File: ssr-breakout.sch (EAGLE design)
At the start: 15 parts, among them U1 DS2413P

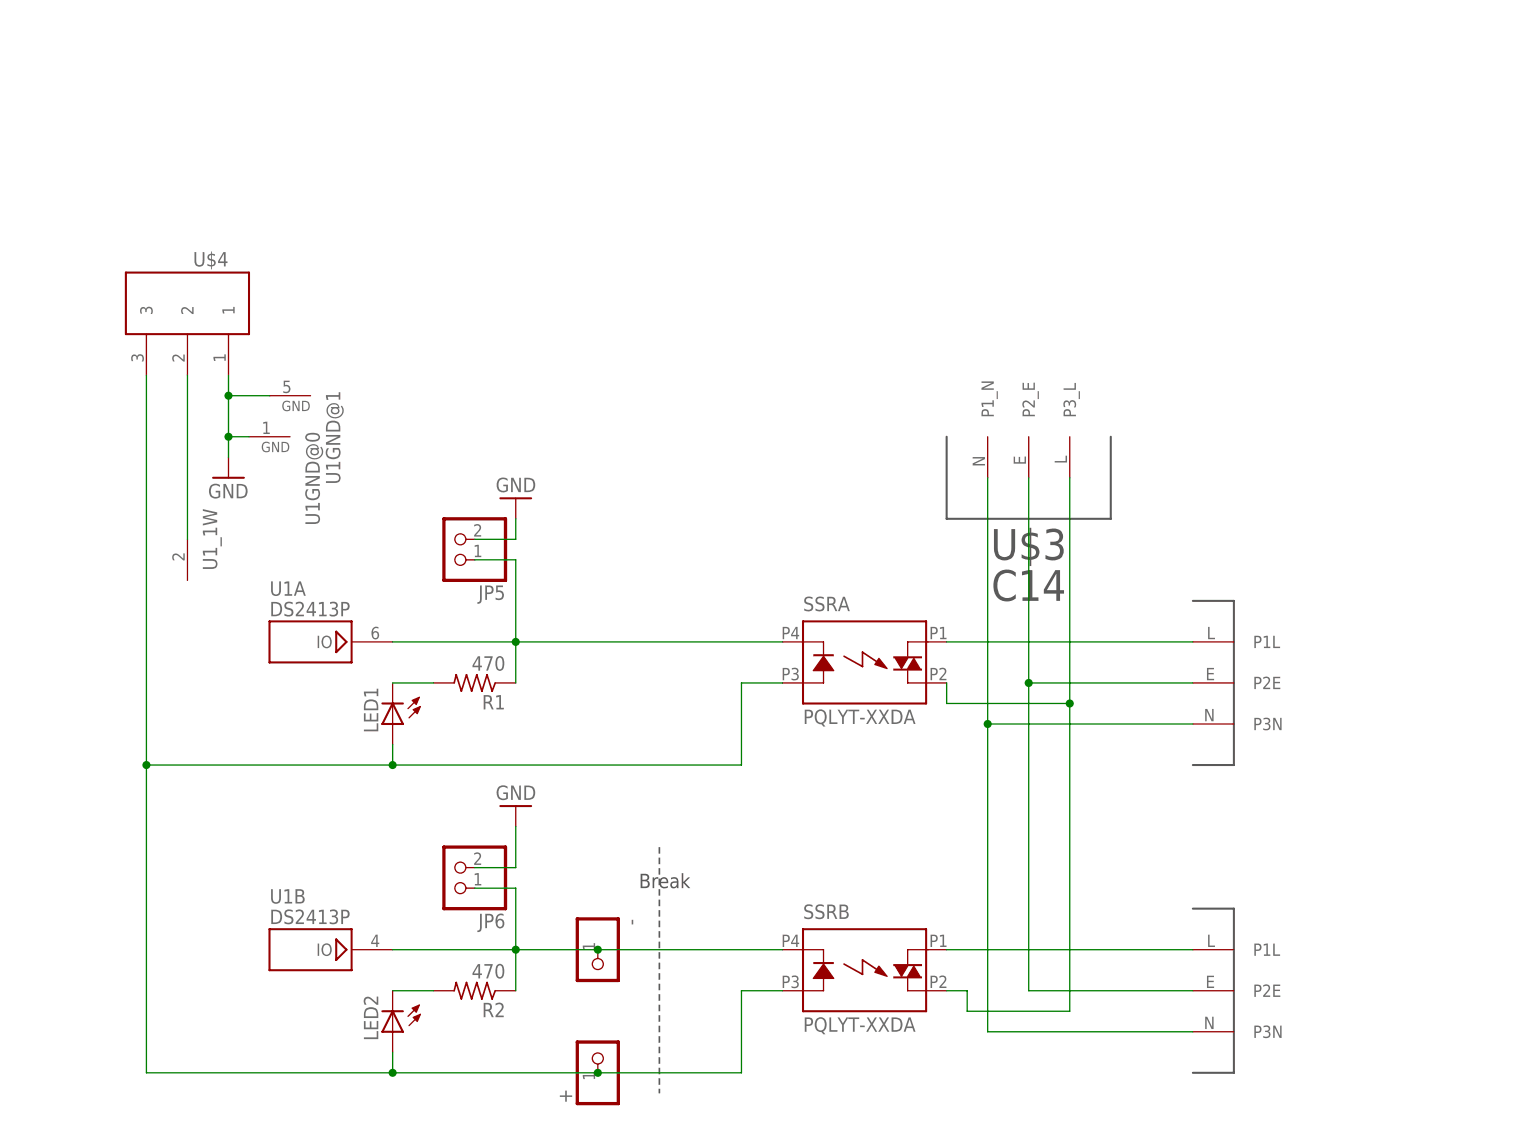
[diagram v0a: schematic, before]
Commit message: Small updates to layout to fit PQLYT SSR
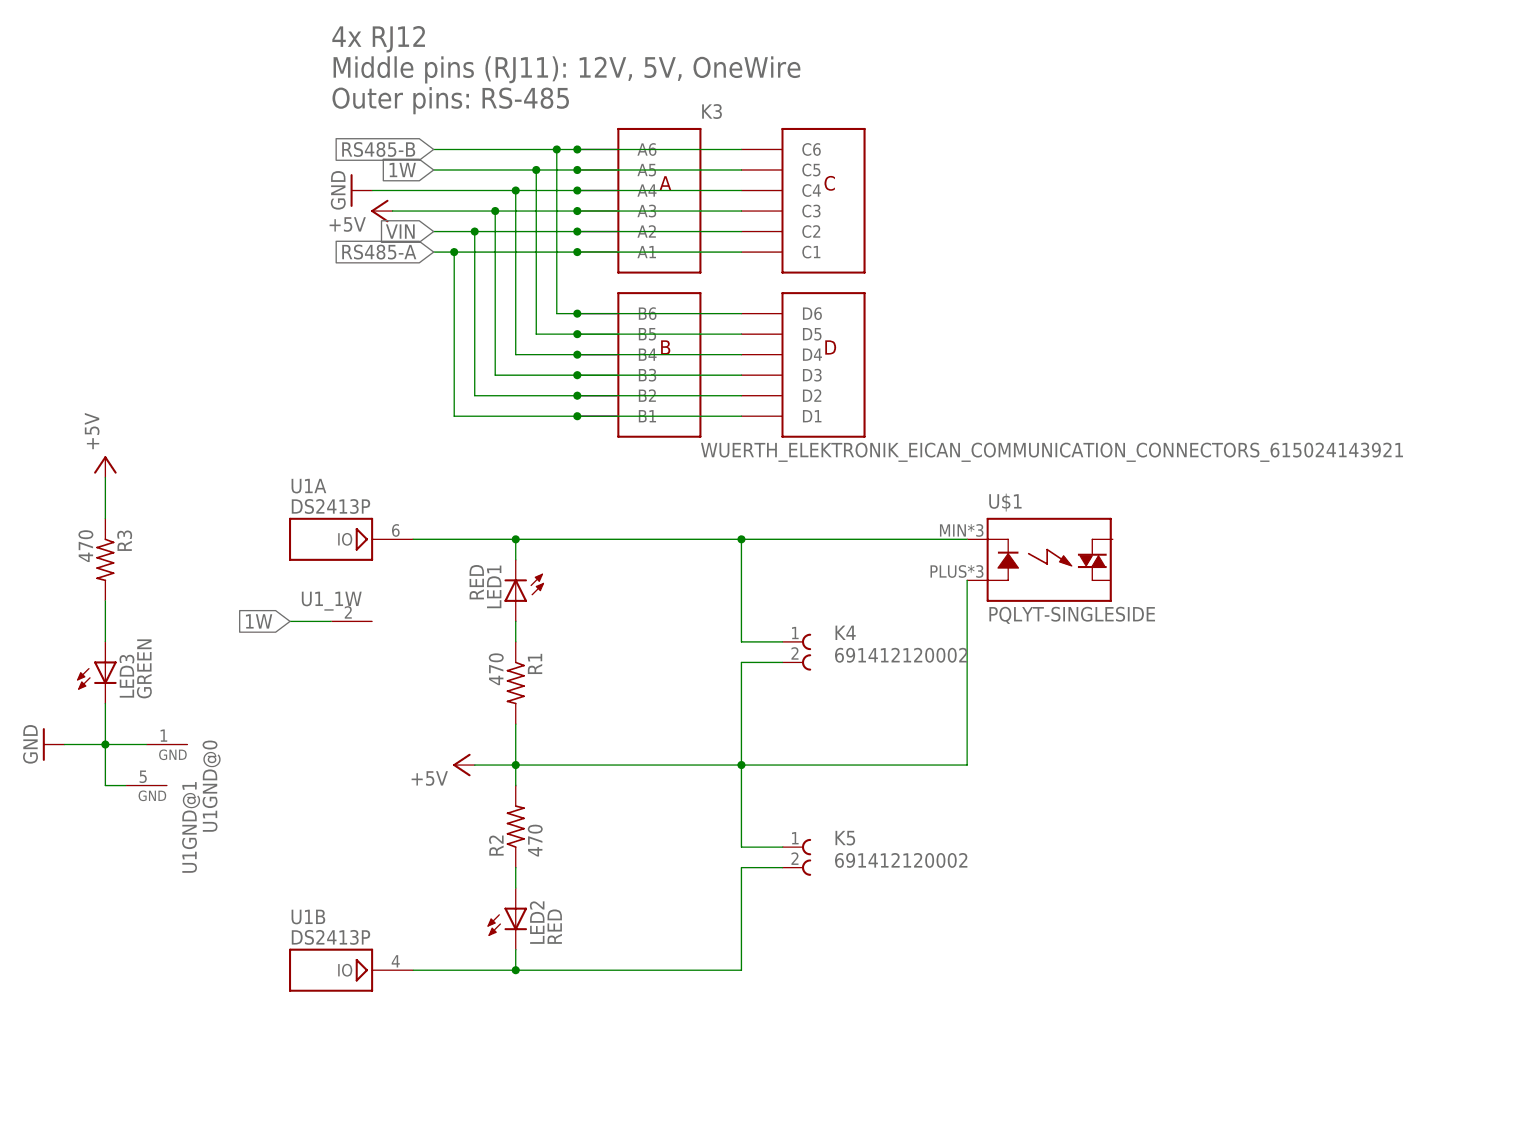
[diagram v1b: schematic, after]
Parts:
- removed +, -: (no value), adafruit:PINHD-1X1CB
- removed JP5, JP6: (no value), pinhead:PINHD-1X2
- removed SSRA, SSRB: PQLYT-XXDA, brewpi:PQLYT-XXDA
- removed U$3: C14, brewpi:C14
- removed U$4: 3.5MM3PHORIZONTAL, elcojacobs:3.5MM3PHORIZONTAL
- removed U$5, U$6: C13, brewpi:C13
- added K3: WUERTH_ELEKTRONIK_EICAN_COMMUNICATION_CONNECTORS_6150241439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, brewpi-spark-shield-revA-v04:WUERTH_ELEKTRONIK_EICAN_COMMUNICATION_CONNECTORS_615024143921
- added K4, K5: 691412120002, Wuerth_Elektronik_eiCan_Terminal_Blocks_Connectors:691412120002
- added LED3: GREEN, brewpi-spark-shield-revA-v04:SPARKFUN-LED_LED-BLUE1206
- added R3: 470, adafruit:R-US_R0805
- added U$1: PQLYT-SINGLESIDE, brewpi:PQLYT-SINGLESIDE
- LED1, LED2: value (none) -> RED; device adafruit:LEDCHIPLED_0805 -> brewpi-spark-shield-revA-v04:SPARKFUN-LED_LED-BLUE1206
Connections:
- removed net N$10: SSRB.DS1, U$6.P1L
- removed net N$13: U$3.P1_N, U$5.P3N, U$6.P3N
- removed net N$6: SSRA.DS1, U$5.P1L
- removed net N$7: SSRA.DS2, SSRB.DS2, U$3.P3_L
- removed net N$8: U$4.2, U1_1W.1W
- removed net N$9: U$3.P2_E, U$5.P2E, U$6.P2E
- new net +5V: K3.A3, K3.B3, K3.C3, K3.D3, K4.2, K5.1, R1.2, R2.2, R3.1, U$1.A
- new net 1W: K3.A5, K3.B5, K3.C5, K3.D5, U1_1W.1W
- new net RS485-A: K3.A1, K3.B1, K3.C1, K3.D1
- new net RS485-B: K3.A6, K3.B6, K3.C6, K3.D6
- new net VIN: K3.A2, K3.B2, K3.C2, K3.D2
- net GND: now also K3.A4, K3.B4, K3.C4, K3.D4, LED3.C; no longer JP5.2, JP6.2, U$4.1
- net N$1: now also K4.1, LED1.C, U$1.K; no longer JP5.1, R1.1, SSRA.K
- net N$2: now also LED1.A, R1.1; no longer LED1.C, R1.2
- net N$3: now also LED2.A, R2.1; no longer LED2.C, R2.2
- net N$4: now also K5.2, LED2.C; no longer -.1, JP6.1, R2.1, SSRB.K
- net N$5: now also LED3.A, R3.2; no longer +.1, LED1.A, LED2.A, SSRA.A, SSRB.A, U$4.3
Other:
- note added: "4x RJ12 Middle pins (RJ11): 12V, 5V, OneWire Outer pins: RS-485"
- note removed: "Break"
- moved on the sheet: LED1, LED2, R1, R2, U1A, U1B, U1GND@0, U1GND@1, U1_1W
